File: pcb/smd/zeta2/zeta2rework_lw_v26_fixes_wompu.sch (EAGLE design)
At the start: 80 parts, among them U5 DS18B20U+

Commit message: version 3 of pcb should be finihsed now
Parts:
- removed 3.3V_CONF: NCP1117LPST33T3G, NCP1117LPST33T3G:NCP1117LPST33T3G
- removed BOOTCONFIG: (no value), special:SW_DIP-2
- removed C11, C18, C21: 0.1µF, rcl:C-EUC1206
- removed C20: 10nf, rcl:C-EUC1206
- removed IRLML1, IRLML2502: (no value), zetex:NMOSSOT23
- removed MPU6050: MPU-6050, MPU-6050:MPU-6050
- removed Q9: (no value), semicon-smd-ipc:NPN-TRANSISTOR_SOT23
- removed R11, R15: 132k, rcl:R-EU_R0603
- removed R18: 500, rcl:R-EU_R0603
- removed SCL, SDA: TPSQTP20R, testpad:TPSQTP20R
- added 1.8V_CONV: MCP1700T-1802E/TT, MCP1700T-2102E_TT:MCP1700T-2102E/TT
- added 3.3V_CONV: NCP1117LPST33T3G, NCP1117LPST33T3G:NCP1117LPST33T3G
- added C1: 100nF, rcl:C-EUC1206
- added C14: 1µF, rcl:C-EUC1206
- added C6, C7, C8: 0.1nF, rcl:C-EUC1206
- added J1: B4B-ZR(LF)(SN), B4B-ZR(LF)(SN):B4B-ZR(LF)(SN)
- added M1, M2, M3: IRLML2502, IRLML2502TRPBF:IRLML2502TRPBF
- added R1, R2: 10k, rcl:R-EU_R0603
- added R6: 22R, rcl:R-EU_R0603
- added U3: ICM-20948, ICM-20948:ICM-20948
- C10, C12, C3, C34, C43: device rcl:CPOL-EUUD-4X5,8 -> rcl:CPOL-EUUD-5X5,8
- C17: value 2,2nF -> 1µF
- R10, R12, R14, R4, R7, R8: value 100k -> 10k
- R3: value 220R -> 0R
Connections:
- removed net BOOT0: BOOTCONFIG.2, R15.2, STM32F103CB.BOOT0
- removed net BOOT1: BOOTCONFIG.1, R11.2, STM32F103CB.PB2
- removed net BOOT2: RPI_ZERO.29
- removed net BOOT3: RPI_ZERO.27
- removed net MPU_INT: MPU6050.INT
- removed net N$19: Q9.B, R18.2
- removed net N$20: Q9.E, R3.1
- removed net N$34: C17.1, MPU6050.CPOUT
- removed net N$36: C21.1, MPU6050.REGOUT
- new net +1.8V: 1.8V_CONV.VOUT, C14.1, C8.1, U3.VDDIO
- new net INT_MD_1: J1.3, STM32F103CB.PB10
- new net INT_MD_2: J1.2, STM32F103CB.PB11
- new net N$10: M3.G, R6.2
- new net N$5: R1.1, STM32F103CB.BOOT0
- new net N$8: C7.1, U3.REGOUT
- new net N$9: FRONTLIGHT.2, M3.D
- net +3V3: now also 1.8V_CONV.VIN, 3.3V_CONV.OUTPUT, C17.1, C6.1, R2.2, U3.VDD; no longer 3.3V_CONF.OUTPUT, BOOTCONFIG.3, BOOTCONFIG.4, C18.1, C20.1, MPU6050.VDD, MPU6050.VLOGIC
- net +5V: now also 3.3V_CONV.INPUT, C15.1, J1.4, R3.1; no longer C11.1, Q9.C
- net +8V: no longer 3.3V_CONF.INPUT, C15.1
- net FRONT_LIGHT: now also R6.1; no longer R18.1
- net GND: now also 1.8V_CONV.GND, 3.3V_CONV.GND, C1.2, C14.2, C6.2, C7.2, C8.2, J1.1, M1.S, M2.S, M3.S, R1.2, U3.GND; no longer 3.3V_CONF.GND, C11.2, C18.2, C20.2, C21.2, FRONTLIGHT.2, IRLML1.S, IRLML2502.S, MPU6050.AD0, MPU6050.CLKIN, MPU6050.FSYNC, MPU6050.GND, R11.1, R15.1
- net N$37: now also M2.G; no longer IRLML2502.G
- net N$38: now also M1.G; no longer IRLML1.G
- net N$39: now also M1.D; no longer IRLML1.D
- net N$55: now also M2.D; no longer IRLML2502.D
- net NRST: now also C1.1, R2.1
- net SCL: now also I2C.1, U3.SCL/SCLK; no longer I2C.2, MPU6050.SCL, SCL.TP
- net SDA: now also I2C.2, U3.SDA/SDI; no longer I2C.1, MPU6050.SDA, SDA.TP
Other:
- moved on the sheet: 3.3V, 5V_CONV, C10, C12, C13, C15, C16, C17, C2, C23, C24, C27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

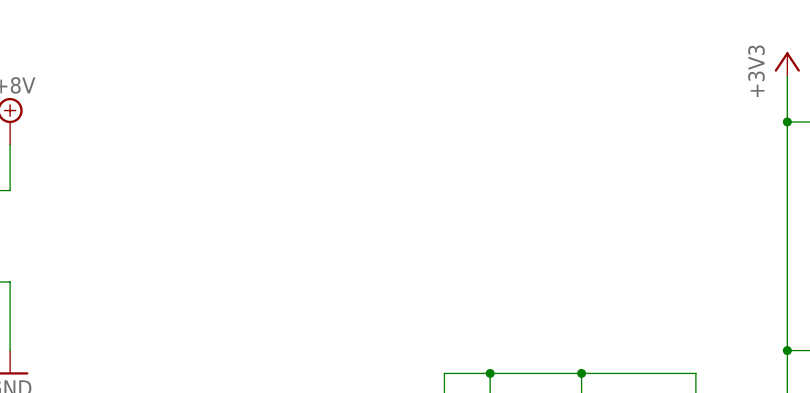
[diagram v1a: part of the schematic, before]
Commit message: moved pwr in, added smd LED
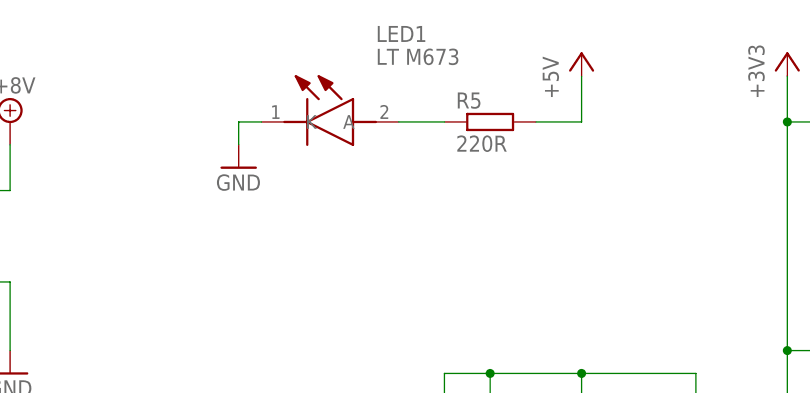
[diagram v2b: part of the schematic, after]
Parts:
- added LED1: LT M673, LT_M673-N1R2-25:LT_M673-N1R2-25
- added R5: 220R, rcl:R-EU_R0603
- C27: device rcl:CPOL-EUUD-4X5,8 -> rcl:CPOL-EUUD-5X5,8
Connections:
- new net N$7: LED1.A, R5.1
- net +5V: now also R5.2
- net GND: now also LED1.K
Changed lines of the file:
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@@
 <grid distance="0.1" unitdist="inch" unit="inch" style="lines" multiple="1" display="no" altdistance="0.01" altunitdist="inch" altunit="inch"/>
 <layers>
-<layer number="1" name="Top" color="4" fill="1" visible="no" active="no"/>
-<layer number="16" name="Bottom" color="1" fill="1" visible="no" active="no"/>
-<layer number="17" name="Pads" color="2" fill="1" visible="no" active="no"/>
-<layer number="18" name="Vias" color="2" fill="1" visible="no" active="no"/>
-<layer number="19" name="Unrouted" color="6" fill="1" visible="no" active="no"/>
-<layer number="20" name="Dimension" color="24" fill="1" visible="no" active="no"/>
-<layer number="21" name="tPlace" color="7" fill="1" visible="no" active="no"/>
-<layer number="22" name="bPlace" color="7" fill="1" visible="no" active="no"/>
-<layer number="23" name="tOrigins" color="15" fill="1" visible="no" active="no"/>
-<layer number="24" name="bOrigins" color="15" fill="1" visible="no" active="no"/>
-<layer number="25" name="tNames" color="7" fill="1" visible="no" active="no"/>
-<layer number="26" name="bNames" color="7" fill="1" visible="no" active="no"/>
-<layer number="27" name="tValues" color="7" fill="1" visible="no" active="no"/>
-<layer number="28" name="bValues" color="7" fill="1" visible="no" active="no"/>
+<layer number="1" name="Top" color="4" fill="1" visible="yes" active="no"/>
+<layer number="16" name="Bottom" color="1" fill="1" visible="yes" active="no"/>
+<layer number="17" name="Pads" color="2" fill="1" visible="yes" active="no"/>
+<layer number="18" name="Vias" color="2" fill="1" visible="yes" active="no"/>
+<layer number="19" name="Unrouted" color="6" fill="1" visible="yes" active="no"/>
+<layer number="20" name="Dimension" color="24" fill="1" visible="yes" active="no"/>
+<layer number="21" name="tPlace" color="7" fill="1" visible="yes" active="no"/>
+<layer number="22" name="bPlace" color="7" fill="1" visible="yes" active="no"/>
+<layer number="23" name="tOrigins" color="15" fill="1" visible="yes" active="no"/>
+<layer number="24" name="bOrigins" color="15" fill="1" visible="yes" active="no"/>
+<layer number="25" name="tNames" color="7" fill="1" visible="yes" active="no"/>
+<layer number="26" name="bNames" color="7" fill="1" visible="yes" active="no"/>
+<layer number="27" name="tValues" color="7" fill="1" visible="yes" active="no"/>
+<layer number="28" name="bValues" color="7" fill="1" visible="yes" active="no"/>
 <layer number="29" name="tStop" color="7" fill="3" visible="no" active="no"/>
 <layer number="30" name="bStop" color="7" fill="6" visible="no" active="no"/>
@@
 <layer number="35" name="tGlue" color="7" fill="4" visible="no" active="no"/>
 <layer number="36" name="bGlue" color="7" fill="5" visible="no" active="no"/>
-<layer number="37" name="tTest" color="7" fill="1" visible="no" active="no"/>
-<layer number="38" name="bTest" color="7" fill="1" visible="no" active="no"/>
+<layer number="37" name="tTest" color="7" fill="1" visible="yes" active="no"/>
+<layer number="38" name="bTest" color="7" fill="1" visible="yes" active="no"/>
 <layer number="39" name="tKeepout" color="4" fill="11" visible="no" active="no"/>
 <layer number="40" name="bKeepout" color="1" fill="11" visible="no" active="no"/>
@@
 <layer number="44" name="Drills" color="7" fill="1" visible="no" active="no"/>
 <layer number="45" name="Holes" color="7" fill="1" visible="no" active="no"/>
-<layer number="46" name="Milling" color="3" fill="1" visible="no" active="no"/>
-<layer number="47" name="Measures" color="7" fill="1" visible="no" active="no"/>
-<layer number="48" name="Document" color="7" fill="1" visible="no" active="no"/>
-<layer number="49" name="Reference" color="7" fill="1" visible="no" active="no"/>
-<layer number="50" name="dxf" color="7" fill="1" visible="no" active="no"/>
-<layer number="51" name="tDocu" color="7" fill="1" visible="no" active="no"/>
-<layer number="52" name="bDocu" color="7" fill="1" visible="no" active="no"/>
-<layer number="53" name="tGND_GNDA" color="7" fill="9" visible="no" active="no"/>
-<layer number="54" name="bGND_GNDA" color="1" fill="9" visible="no" active="no"/>
-<layer number="56" name="wert" color="7" fill="1" visible="no" active="no"/>
-<layer number="57" name="tCAD" color="7" fill="1" visible="no" active="no"/>
-<layer number="59" name="tCarbon" color="7" fill="1" visible="no" active="no"/>
-<layer number="60" name="bCarbon" color="7" fill="1" visible="no" active="no"/>
+<layer number="46" name="Milling" color="3" fill="1" visible="yes" active="no"/>
+<layer number="47" name="Measures" color="7" fill="1" visible="yes" active="no"/>
+<layer number="48" name="Document" color="7" fill="1" visible="yes" active="no"/>
+<layer number="49" name="Reference" color="7" fill="1" visible="yes" active="no"/>
+<layer number="50" name="dxf" color="7" fill="1" visible="yes" active="no"/>
+<layer number="51" name="tDocu" color="7" fill="1" visible="yes" active="no"/>
+<layer number="52" name="bDocu" color="7" fill="1" visible="yes" active="no"/>
+<layer number="53" name="tGND_GNDA" color="7" fill="9" visible="yes" active="no"/>
+<layer number="54" name="bGND_GNDA" color="1" fill="9" visible="yes" active="no"/>
+<layer number="56" name="wert" color="7" fill="1" visible="yes" active="no"/>
+<layer number="57" name="tCAD" color="7" fill="1" visible="yes" active="no"/>
+<layer number="59" name="tCarbon" color="7" fill="1" visible="yes" active="no"/>
+<layer number="60" name="bCarbon" color="7" fill="1" visible="yes" active="no"/>
 <layer number="88" name="SimResults" color="9" fill="1" visible="yes" active="yes"/>
 <layer number="89" name="SimProbes" color="9" fill="1" visible="yes" active="yes"/>
@@
 <part name="GND16" library="supply1" library_urn="urn:adsk.eagle:library:371" deviceset="GND" device=""/>
 <part name="P+13" library="supply1" library_urn="urn:adsk.eagle:library:371" deviceset="V+" device=""/>
-<part name="C27" library="rcl" library_urn="urn:adsk.eagle:library:334" deviceset="CPOL-EU" device="UD-4X5,8" package3d_urn="urn:adsk.eagle:package:23474/1" value="100µF"/>
+<part name="C27" library="rcl" library_urn="urn:adsk.eagle:library:334" deviceset="CPOL-EU" device="UD-5X5,8" package3d_urn="urn:adsk.eagle:package:23470/1" value="100µF"/>
 <part name="5V_CONV" library="diy-modules" deviceset="DC-DC-STEP-DOWN-MP2307" device=""/>
 <part name="GND27" library="supply1" library_urn="urn:adsk.eagle:library:371" deviceset="GND" device=""/>
@@
 <part name="M3" library="IRLML2502TRPBF" deviceset="IRLML2502TRPBF" device="" value="IRLML2502"/>
 <part name="M1" library="IRLML2502TRPBF" deviceset="IRLML2502TRPBF" device="" value="IRLML2502"/>
+<part name="LED1" library="LT_M673-N1R2-25" deviceset="LT_M673-N1R2-25" device="" value="LT M673"/>
+<part name="R5" library="rcl" library_urn="urn:adsk.eagle:library:334" deviceset="R-EU_" device="R0603" package3d_urn="urn:adsk.eagle:package:23555/2" value="220R"/>
+<part name="GND28" library="supply1" library_urn="urn:adsk.eagle:library:371" deviceset="GND" device=""/>
+<part name="P+9" library="supply1" library_urn="urn:adsk.eagle:library:371" deviceset="+5V" device=""/>
 </parts>
 <sheets>
@@
 <instance part="M3" gate="G$1" x="-226.06" y="-177.8"/>
 <instance part="M1" gate="G$1" x="-157.48" y="-185.42"/>
+<instance part="LED1" gate="G$1" x="-114.3" y="0"/>
+<instance part="R5" gate="G$1" x="-88.9" y="0"/>
+<instance part="GND28" gate="1" x="-116.84" y="-5.08"/>
+<instance part="P+9" gate="1" x="-78.74" y="7.62"/>
 </instances>
 <busses>
@@
 <wire x1="-129.54" y1="-68.58" x2="-129.54" y2="-63.5" width="0.1524" layer="91"/>
 </segment>
+<segment>
+<pinref part="GND28" gate="1" pin="GND"/>
+<pinref part="LED1" gate="G$1" pin="K"/>
+<wire x1="-116.84" y1="-2.54" x2="-116.84" y2="0" width="0.1524" layer="91"/>
+<wire x1="-116.84" y1="0" x2="-114.3" y2="0" width="0.1524" layer="91"/>
+</segment>
 </net>
 <net name="V+" class="0">
@@
 <pinref part="P+6" gate="1" pin="+5V"/>
 </segment>
+<segment>
+<pinref part="R5" gate="G$1" pin="2"/>
+<wire x1="-83.82" y1="0" x2="-78.74" y2="0" width="0.1524" layer="91"/>
+<pinref part="P+9" gate="1" pin="+5V"/>
+<wire x1="-78.74" y1="0" x2="-78.74" y2="5.08" width="0.1524" layer="91"/>
+</segment>
 </net>
 <net name="SCL" class="0">
@@
 </segment>
 </net>
+<net name="N$7" class="0">
+<segment>
+<pinref part="LED1" gate="G$1" pin="A"/>
+<pinref part="R5" gate="G$1" pin="1"/>
+<wire x1="-93.98" y1="0" x2="-99.06" y2="0" width="0.1524" layer="91"/>
+</segment>
+</net>
